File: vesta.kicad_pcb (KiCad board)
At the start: 4 copper layers, 43 x 61.1 mm, 62 parts, among them J1 Solar Panel, J2 Solar Panel, J3 Conn_ARM_SWD_TagConnect_TC203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, U1 STM32WL55CCU6, U2 BQ24074RGTR, U3 TPS63900DSKR, U4 BME688_C3664478, U6 PE4259-63, X1 Q13FC1350000400, X2 X201632MMB4SI

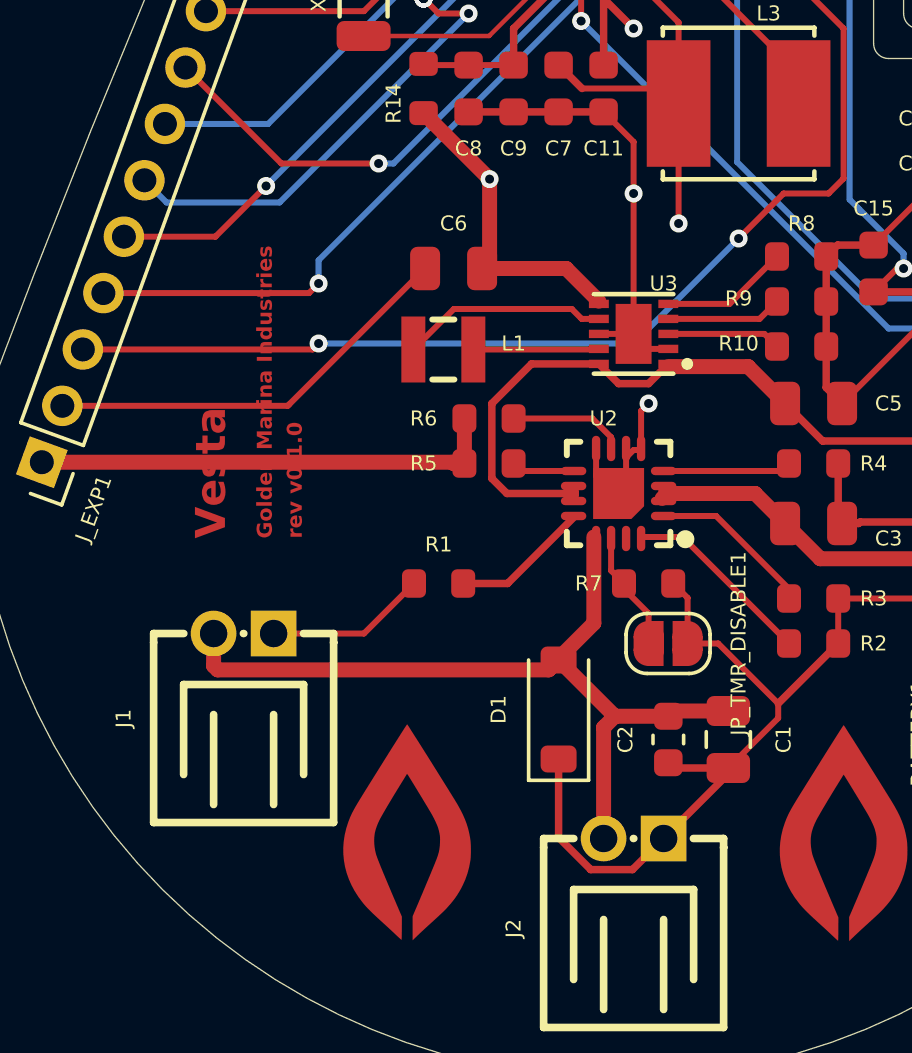
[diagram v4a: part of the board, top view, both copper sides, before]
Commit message: feat: reverting the polarity on the batteries inputs
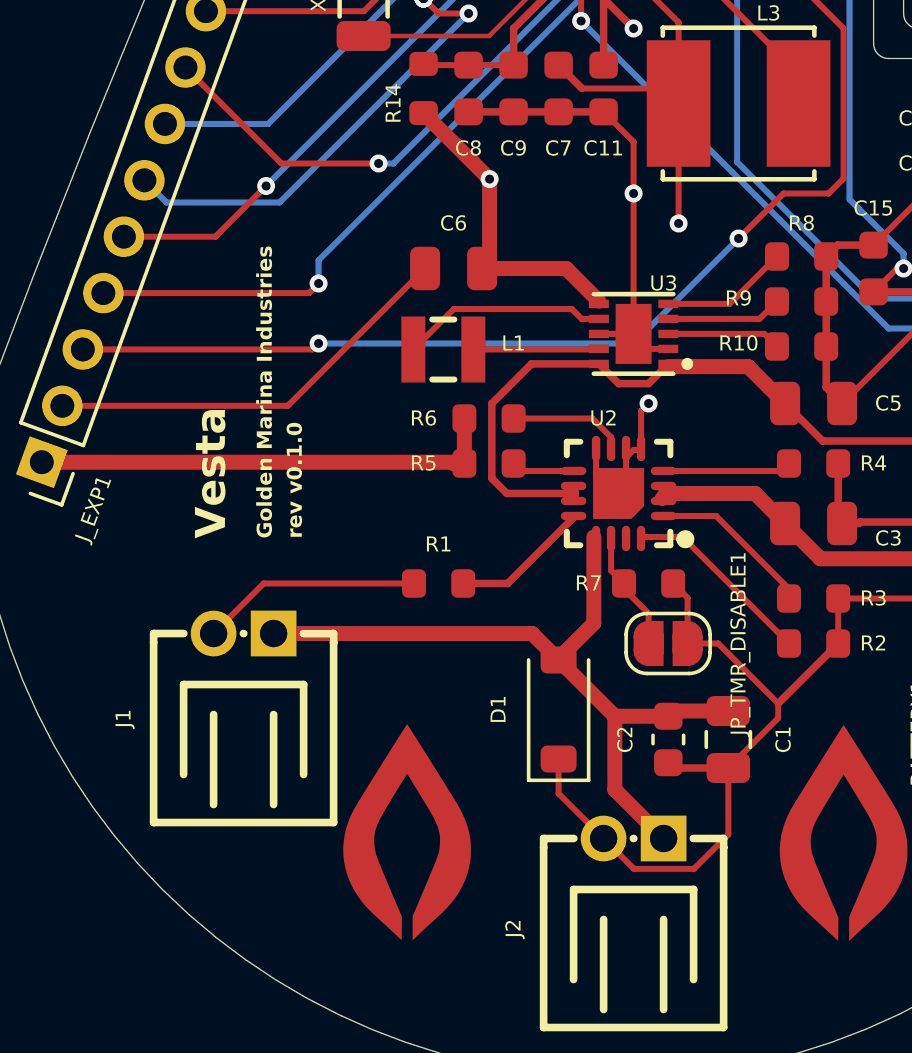
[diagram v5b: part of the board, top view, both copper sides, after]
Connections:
- J1 pad 1: GND -> /VIN_SOLAR
- J1 pad 2: /VIN_SOLAR -> GND
- J2 pad 1: GND -> /VIN_SOLAR
- J2 pad 2: /VIN_SOLAR -> GND
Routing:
- net GND: track 157.7 -> 160.2 mm
- net /VIN_SOLAR: track 28.1 -> 25.7 mm
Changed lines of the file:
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@@
 			(layers "*.Cu" "*.Mask")
 			(remove_unused_layers no)
-			(net "GND")
+			(net "/VIN_SOLAR")
 			(pinfunction "Pin_1_1")
 			(pintype "passive")
@@
 			(layers "*.Cu" "*.Mask")
 			(remove_unused_layers no)
-			(net "/VIN_SOLAR")
+			(net "GND")
 			(pinfunction "Pin_2_2")
 			(pintype "passive")
@@
 			(layers "*.Cu" "*.Mask")
 			(remove_unused_layers no)
-			(net "GND")
+			(net "/VIN_SOLAR")
 			(pinfunction "Pin_1_1")
 			(pintype "passive")
@@
 			(layers "*.Cu" "*.Mask")
 			(remove_unused_layers no)
-			(net "/VIN_SOLAR")
+			(net "GND")
 			(pinfunction "Pin_2_2")
 			(pintype "passive")
@@
 	(gr_text "Golden Marina Industries"
 		(at 28.5 61 90)
-		(layer "F.Cu")
+		(layer "F.SilkS")
 		(effects
 			(font
@@
 	(gr_text "rev v0.1.0"
 		(at 29.5 61 90)
-		(layer "F.Cu")
+		(layer "F.SilkS")
 		(effects
 			(font
@@
 	(gr_text "Vesta"
 		(at 27 61 90)
-		(layer "F.Cu")
+		(layer "F.SilkS")
 		(effects
 			(font
@@
 	)
 	(segment
-		(start 31.512474 64.167526)
-		(end 33.18 62.5)
-		(width 0.2)
-		(layer "F.Cu")
-		(net "GND")
-	)
-	(segment
 		(start 44.28 28.04)
 		(end 44.32 28)
@@
 	)
 	(segment
+		(start 39.5 71)
+		(end 40.512001 72.012001)
+		(width 0.2)
+		(layer "F.Cu")
+		(net "GND")
+	)
+	(segment
 		(start 42.3 64.5)
 		(end 42.3 62.98)
@@
 	)
 	(segment
+		(start 43.657607 70.866395)
+		(end 43.657607 68.650076)
+		(width 0.2)
+		(layer "F.Cu")
+		(net "GND")
+	)
+	(segment
 		(start 51.832474 63)
 		(end 53 64.167526)
@@
 	)
 	(segment
+		(start 38 69.5)
+		(end 38 68.350076)
+		(width 0.2)
+		(layer "F.Cu")
+		(net "GND")
+	)
+	(segment
 		(start 50.36 49.36)
 		(end 48.5 51.22)
@@
 	)
 	(segment
+		(start 33.18 62.5)
+		(end 28.167526 62.5)
+		(width 0.2)
+		(layer "F.Cu")
+		(net "GND")
+	)
+	(segment
 		(start 54.474003 43.474003)
 		(end 54.414135 43.474003)
@@
 	)
 	(segment
+		(start 28.167526 62.5)
+		(end 26.5 64.167526)
+		(width 0.2)
+		(layer "F.Cu")
+		(net "GND")
+	)
+	(segment
 		(start 28.972151 56.577849)
 		(end 29.025 56.525)
@@
 	)
 	(segment
+		(start 40.512001 72.012001)
+		(end 42.512001 72.012001)
+		(width 0.2)
+		(layer "F.Cu")
+		(net "GND")
+	)
+	(segment
 		(start 43.657607 68.650076)
 		(end 41.832607 68.650076)
@@
 	)
 	(segment
+		(start 42.512001 72.012001)
+		(end 43.657607 70.866395)
+		(width 0.2)
+		(layer "F.Cu")
+		(net "GND")
+	)
+	(segment
 		(start 35.774955 31.225045)
 		(end 35.5 31.5)
@@
 	)
 	(segment
-		(start 43.657607 68.842393)
-		(end 41.5 71)
-		(width 0.25)
-		(layer "F.Cu")
-		(net "GND")
-	)
-	(segment
 		(start 47.32 58.5)
 		(end 47.32 60.37)
@@
 	)
 	(segment
-		(start 37.66002 30.620016)
-		(end 37.66002 31.310135)
+		(start 39.5 71)
+		(end 38 69.5)
 		(width 0.2)
 		(layer "F.Cu")
@@
 	)
 	(segment
-		(start 28.5 64.167526)
-		(end 31.512474 64.167526)
+		(start 37.66002 30.620016)
+		(end 37.66002 31.310135)
 		(width 0.2)
 		(layer "F.Cu")
@@
 	)
 	(segment
-		(start 41.5 71)
-		(end 40.462999 72.037001)
-		(width 0.25)
-		(layer "F.Cu")
-		(net "GND")
-	)
-	(segment
 		(start 40.499873 49.5)
 		(end 40.499873 47.779873)
@@
 	)
 	(segment
-		(start 40.462999 72.037001)
-		(end 39.07046 72.037001)
-		(width 0.25)
-		(layer "F.Cu")
-		(net "GND")
-	)
-	(segment
 		(start 46.92 51.6)
 		(end 46.92 54.6)
@@
 	)
 	(segment
-		(start 39.07046 72.037001)
-		(end 38 70.966541)
-		(width 0.25)
-		(layer "F.Cu")
-		(net "GND")
-	)
-	(segment
 		(start 32.950089 35.049911)
 		(end 33 35)
@@
 	)
 	(segment
-		(start 38 70.966541)
-		(end 38 68.350076)
-		(width 0.25)
-		(layer "F.Cu")
-		(net "GND")
-	)
-	(segment
 		(start 51.380671 43.5)
 		(end 54.388138 43.5)
@@
 	)
 	(segment
-		(start 26.634369 65.379527)
-		(end 26.5 65.245158)
+		(start 37.11745 64.167526)
+		(end 38 65.050076)
+		(width 0.5)
+		(layer "F.Cu")
+		(net "/VIN_SOLAR")
+	)
+	(segment
+		(start 39.875 69.375)
+		(end 39.875 66.925076)
 		(width 0.5)
 		(layer "F.Cu")
@@
 	)
 	(segment
-		(start 38 65.050076)
-		(end 37.670549 65.379527)
-		(width 0.5)
-		(layer "F.Cu")
-		(net "/VIN_SOLAR")
-	)
-	(segment
-		(start 39.5 67.300076)
-		(end 39.875 66.925076)
+		(start 41.5 71)
+		(end 39.875 69.375)
 		(width 0.5)
 		(layer "F.Cu")
@@
 	)
 	(segment
-		(start 37.670549 65.379527)
-		(end 26.634369 65.379527)
-		(width 0.5)
-		(layer "F.Cu")
-		(net "/VIN_SOLAR")
-	)
-	(segment
-		(start 26.5 65.245158)
-		(end 26.5 64.167526)
-		(width 0.5)
-		(layer "F.Cu")
-		(net "/VIN_SOLAR")
-	)
-	(segment
-		(start 39.5 71)
-		(end 39.5 67.300076)
+		(start 28.5 64.167526)
+		(end 37.11745 64.167526)
 		(width 0.5)
 		(layer "F.Cu")
